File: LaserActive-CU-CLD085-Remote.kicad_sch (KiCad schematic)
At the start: 0 parts

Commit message: Initial start
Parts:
- added C1: 100nF, Capacitor_THT:C_Disc_D4.3mm_W1.9mm_P5.00mm, symbol Device:C_Small
- added C2, C3: 10pF, Capacitor_THT:C_Disc_D3.0mm_W1.6mm_P2.50mm, symbol Device:C_Small
- added C4: 47uF, Capacitor_THT:CP_Radial_D5.0mm_P2.00mm, symbol Device:C_Polarized_Small
- added C5: C_Small, Capacitor_THT:C_Disc_D4.3mm_W1.9mm_P5.00mm, symbol Device:C_Small
- added D1: D_Dual_CommonAnode_AKK, Package_TO_SOT_THT:TO-126-3_Vertical, symbol Device:D_Dual_CommonAnode_AKK
- added D3: IRL81A, LED_THT:LED_SideEmitter_Rectangular_W4.5mm_H1.6mm, symbol LED:IRL81A
- added IC1: D6600CS, Package_DIP:DIP-20_W7.62mm_Socket_LongPads, symbol Pioneer:D6600CS
- added K0, K1, K10, K11, K12, K16, K18, K19, K2, K20, K24, K25, K26, K27, K28, K29, K3, K32, K33, K34, K35, K36, K4, K7: Button, Button_Switch_SMD:SW_SPST_CK_KXT3, symbol Switch:SW_Push
- added Q1: NPN, Package_TO_SOT_THT:TO-220-3_Vertical, symbol Simulation_SPICE:NPN
- added R1: 220, Resistor_THT:R_Axial_DIN0204_L3.6mm_D1.6mm_P5.08mm_Horizontal, symbol Device:R_Small
- added X1: Crystal, Crystal:Crystal_HC18-U_Vertical, symbol Device:Crystal
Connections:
- new net: C3.2, IC1.8 (OSC-IN), X1.1
- new net: C2.2, IC1.7 (OSC-OUT), X1.2
- new net: C1.1, IC1.10 (AC)
- new net: D1.2 (K), IC1.3 (S-IN)
- new net: IC1.5 (REM), Q1.2 (B)
- new net: D3.2 (A), Q1.1 (C)
- new net: D3.1 (K), R1.2
- new net COL_1: IC1.14 (K_I0)
- new net COL_2: IC1.13 (K_I1)
- new net COL_3: IC1.12 (K_I2), K16.1, K18.1, K19.1, K20.1
- new net COL_4: IC1.11 (K_I3)
- new net GND: C1.2, C2.1, C3.1, C4.2, C5.2, IC1.9 (VSS), Q1.3 (E)
- new net ROW_1: IC1.2 (K_IO0)
- new net ROW_2: IC1.1 (K_IO1)
- new net ROW_3: IC1.20 (K_IO2)
- new net ROW_4: IC1.19 (K_IO3), K16.2
- new net ROW_5: IC1.18 (K_IO4)
- new net ROW_6: IC1.17 (K_IO5)
- new net ROW_7: IC1.16 (K_IO6)
- new net ROW_8: IC1.15 (K_IO7)
- new net VCC: C4.1, C5.1, IC1.6 (VDD), R1.1
- no-connect marks 0 -> 1

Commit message: Updates
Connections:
- net COL_1: now also K16.1, K18.1, K19.1, K20.1
- net COL_3: no longer K16.1, K18.1, K19.1, K20.1
- net ROW_1: now also K16.2
- net ROW_2: now also K10.2, K18.2
- net ROW_4: no longer K16.2
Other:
- moved on the sheet: K10, K16, K18, K19, K2, K20
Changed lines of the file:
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@@
 	)
 	(junction
-		(at 154.94 171.45)
+		(at 147.32 114.3)
 		(diameter 0)
 		(color 0 0 0 0)
 	)
 	(junction
-		(at 154.94 149.86)
+		(at 147.32 92.71)
 		(diameter 0)
 		(color 0 0 0 0)
 	)
 	(junction
-		(at 154.94 161.29)
+		(at 147.32 104.14)
 		(diameter 0)
 		(color 0 0 0 0)
@@
 	(wire
 		(pts
-			(xy 154.94 161.29) (xy 154.94 171.45)
+			(xy 147.32 104.14) (xy 147.32 114.3)
 		)
 		(stroke
@@
 	(wire
 		(pts
-			(xy 154.94 171.45) (xy 154.94 181.61)
+			(xy 147.32 114.3) (xy 147.32 124.46)
 		)
 		(stroke
@@
 	(wire
 		(pts
-			(xy 152.4 149.86) (xy 154.94 149.86)
+			(xy 144.78 92.71) (xy 147.32 92.71)
 		)
 		(stroke
@@
 	(wire
 		(pts
-			(xy 154.94 149.86) (xy 154.94 161.29)
+			(xy 147.32 92.71) (xy 147.32 104.14)
 		)
 		(stroke
@@
 		)
 	)
-	(global_label "COL_3"
-		(shape output)
-		(at 152.4 149.86 180)
+	(global_label "COL_1"
+		(shape input)
+		(at 144.78 92.71 180)
 		(fields_autoplaced yes)
 		(effects
@@
 		)
 		(property "Intersheetrefs" "${INTERSHEET_REFS}"
-			(at 143.6091 149.86 0)
+			(at 135.9891 92.71 0)
 			(effects
 				(font
@@
 		)
 	)
+	(global_label "ROW_2"
+		(shape input)
+		(at 186.69 104.14 0)
+		(fields_autoplaced yes)
+		(effects
+			(font
+				(size 1.27 1.27)
+			)
+			(justify left)
+		)
+		(property "Intersheetrefs" "${INTERSHEET_REFS}"
+			(at 195.9042 104.14 0)
+			(effects
+				(font
+					(size 1.27 1.27)
+				)
+				(justify left)
+				(hide yes)
+			)
+		)
+	)
 	(global_label "ROW_7"
 		(shape output)
@@
 		)
 	)
-	(global_label "ROW_4"
+	(global_label "ROW_1"
 		(shape input)
-		(at 165.1 149.86 0)
+		(at 157.48 92.71 0)
 		(fields_autoplaced yes)
 		(effects
@@
 		)
 		(property "Intersheetrefs" "${INTERSHEET_REFS}"
-			(at 174.3142 149.86 0)
+			(at 166.6942 92.71 0)
 			(effects
 				(font
@@
 		)
 	)
+	(global_label "ROW_2"
+		(shape input)
+		(at 157.48 104.14 0)
+		(fields_autoplaced yes)
+		(effects
+			(font
+				(size 1.27 1.27)
+			)
+			(justify left)
+		)
+		(property "Intersheetrefs" "${INTERSHEET_REFS}"
+			(at 166.6942 104.14 0)
+			(effects
+				(font
+					(size 1.27 1.27)
+				)
+				(justify left)
+				(hide yes)
+			)
+		)
+	)
 	(global_label "ROW_1"
 		(shape output)
@@
 	(symbol
 		(lib_id "Switch:SW_Push")
-		(at 160.02 149.86 0)
+		(at 152.4 92.71 0)
 		(unit 1)
 		(exclude_from_sim no)
@@
 		(fields_autoplaced yes)
 		(property "Reference" "K16"
-			(at 160.02 142.24 0)
+			(at 152.4 85.09 0)
 			(effects
 				(font
@@
 		)
 		(property "Value" "Button"
-			(at 160.02 144.78 0)
+			(at 152.4 87.63 0)
 			(effects
 				(font
@@
 		)
 		(property "Footprint" "Button_Switch_SMD:SW_SPST_CK_KXT3"
-			(at 160.02 144.78 0)
+			(at 152.4 87.63 0)
 			(effects
 				(font
@@
 		)
 		(property "Datasheet" "~"
-			(at 160.02 144.78 0)
+			(at 152.4 87.63 0)
 			(effects
 				(font
@@
 		)
 		(property "Description" "Push button switch, generic, two pins"
-			(at 160.02 149.86 0)
+			(at 152.4 92.71 0)
 			(effects
 				(font
@@
 	(symbol
 		(lib_id "Switch:SW_Push")
-		(at 160.02 171.45 0)
+		(at 152.4 114.3 0)
 		(unit 1)
 		(exclude_from_sim no)
@@
 		(fields_autoplaced yes)
 		(property "Reference" "K19"
-			(at 160.02 163.83 0)
+			(at 152.4 106.68 0)
 			(effects
 				(font
@@
 		)
 		(property "Value" "Button"
-			(at 160.02 166.37 0)
+			(at 152.4 109.22 0)
 			(effects
 				(font
@@
 		)
 		(property "Footprint" "Button_Switch_SMD:SW_SPST_CK_KXT3"
-			(at 160.02 166.37 0)
+			(at 152.4 109.22 0)
 			(effects
 				(font
@@
 		)
 		(property "Datasheet" "~"
-			(at 160.02 166.37 0)
+			(at 152.4 109.22 0)
 			(effects
 				(font
@@
 		)
 		(property "Description" "Push button switch, generic, two pins"
-			(at 160.02 171.45 0)
+			(at 152.4 114.3 0)
 			(effects
 				(font
@@
 	(symbol
 		(lib_id "Switch:SW_Push")
-		(at 160.02 181.61 0)
+		(at 152.4 124.46 0)
 		(unit 1)
 		(exclude_from_sim no)
@@
 		(fields_autoplaced yes)
 		(property "Reference" "K20"
-			(at 160.02 173.99 0)
+			(at 152.4 116.84 0)
 			(effects
 				(font
@@
 		)
 		(property "Value" "Button"
-			(at 160.02 176.53 0)
+			(at 152.4 119.38 0)
 			(effects
 				(font
@@
 		)
 		(property "Footprint" "Button_Switch_SMD:SW_SPST_CK_KXT3"
-			(at 160.02 176.53 0)
+			(at 152.4 119.38 0)
 			(effects
 				(font
@@
 		)
 		(property "Datasheet" "~"
-			(at 160.02 176.53 0)
+			(at 152.4 119.38 0)
 			(effects
 				(font
@@
 		)
 		(property "Description" "Push button switch, generic, two pins"
-			(at 160.02 181.61 0)
+			(at 152.4 124.46 0)
 			(effects
 				(font
@@
 	(symbol
 		(lib_id "Switch:SW_Push")
-		(at 72.39 138.43 0)
+		(at 181.61 104.14 0)
 		(unit 1)
 		(exclude_from_sim no)
@@
 		(fields_autoplaced yes)
 		(property "Reference" "K10"
-			(at 72.39 130.81 0)
+			(at 181.61 96.52 0)
 			(effects
 				(font
@@
 		)
 		(property "Value" "Button"
-			(at 72.39 133.35 0)
+			(at 181.61 99.06 0)
 			(effects
 				(font
@@
 		)
 		(property "Footprint" "Button_Switch_SMD:SW_SPST_CK_KXT3"
-			(at 72.39 133.35 0)
+			(at 181.61 99.06 0)
 			(effects
 				(font
@@
 		)
 		(property "Datasheet" "~"
-			(at 72.39 133.35 0)
+			(at 181.61 99.06 0)
 			(effects
 				(font
@@
 		)
 		(property "Description" "Push button switch, generic, two pins"
-			(at 72.39 138.43 0)
+			(at 181.61 104.14 0)
 			(effects
 				(font
@@
 	(symbol
 		(lib_id "Switch:SW_Push")
-		(at 160.02 161.29 0)
+		(at 152.4 104.14 0)
 		(unit 1)
 		(exclude_from_sim no)
@@
 		(fields_autoplaced yes)
 		(property "Reference" "K18"
-			(at 160.02 153.67 0)
+			(at 152.4 96.52 0)
 			(effects
 				(font
@@
 		)
 		(property "Value" "Button"
-			(at 160.02 156.21 0)
+			(at 152.4 99.06 0)
 			(effects
 				(font
@@
 		)
 		(property "Footprint" "Button_Switch_SMD:SW_SPST_CK_KXT3"
-			(at 160.02 156.21 0)
+			(at 152.4 99.06 0)
 			(effects
 				(font
@@
 		)
 		(property "Datasheet" "~"
-			(at 160.02 156.21 0)
+			(at 152.4 99.06 0)
 			(effects
 				(font
@@
 		)
 		(property "Description" "Push button switch, generic, two pins"
-			(at 160.02 161.29 0)
+			(at 152.4 104.14 0)
 			(effects
 				(font
@@
 	(symbol
 		(lib_id "Switch:SW_Push")
-		(at 95.25 138.43 0)
+		(at 208.28 104.14 0)
 		(unit 1)
 		(exclude_from_sim no)
@@
 		(fields_autoplaced yes)
 		(property "Reference" "K2"
-			(at 95.25 130.81 0)
+			(at 208.28 96.52 0)
 			(effects
 				(font
@@
 		)
 		(property "Value" "Button"
-			(at 95.25 133.35 0)
+			(at 208.28 99.06 0)
 			(effects
 				(font
@@
 		)
 		(property "Footprint" "Button_Switch_SMD:SW_SPST_CK_KXT3"
-			(at 95.25 133.35 0)
+			(at 208.28 99.06 0)
 			(effects
 				(font
@@
 		)
 		(property "Datasheet" "~"
-			(at 95.25 133.35 0)
+			(at 208.28 99.06 0)
 			(effects
 				(font
@@
 		)
 		(property "Description" "Push button switch, generic, two pins"
-			(at 95.25 138.43 0)
+			(at 208.28 104.14 0)
 			(effects
 				(font

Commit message: Update LaserActive-CU-CLD085-Remote.kicad_sch
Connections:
- net COL_1: no longer K16.1, K18.1, K19.1, K20.1
- net COL_2: now also K12.2, K20.2, K4.2
- net COL_3: now also K11.1, K19.2, K3.1
- net COL_4: now also K10.2, K18.2, K2.1
- net ROW_1: now also K0.2
- net ROW_2: now also K1.1; no longer K10.2, K18.2
- net ROW_4: now also K16.1, K18.1, K19.1, K20.1
- net ROW_5: now also K10.1, K11.2, K12.1
- net ROW_6: now also K0.1, K1.2, K2.2, K3.2, K4.1
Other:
- moved on the sheet: K0, K1, K10, K11, K12, K16, K18, K19, K2, K20, K3, K4

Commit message: Updates
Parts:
- renumbered C3 to C2, C2 to C3
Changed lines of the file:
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@@
 		(on_board yes)
 		(dnp no)
-		(property "Reference" "C3"
+		(property "Reference" "C2"
 			(at 27.94 76.708 90)
 			(effects
@@
 			(project "LaserActive-CU-CLD085-Remote"
 				(path "/0003d985-390a-41d3-bb3f-5e7567d09c25"
-					(reference "C3")
+					(reference "C2")
 					(unit 1)
 				)
@@
 		(dnp no)
 		(fields_autoplaced yes)
-		(property "Reference" "C2"
+		(property "Reference" "C3"
 			(at 27.9463 58.42 90)
 			(effects
@@
 			(project "LaserActive-CU-CLD085-Remote"
 				(path "/0003d985-390a-41d3-bb3f-5e7567d09c25"
-					(reference "C2")
-					(unit 1)
-				)
+					(reference "C3")
+					(unit 1)
+				)

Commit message: Update Schematics and PCB
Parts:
- added T1, T2: B+, Connector_PinHeader_2.54mm:PinHeader_1x01_P2.54mm_Vertical, symbol Connector_Generic:Conn_01x01
- C4: footprint Capacitor_THT:CP_Radial_D5.0mm_P2.00mm -> Pioneer:Electrolytic_P2.50mm
- IC1: footprint Package_DIP:DIP-20_W7.62mm_Socket_LongPads -> Pioneer:DIP-20_W7.62mm_P1.76mm
- K0, K1, K10, K11, K12, K16, K18, K19, K2, K20, K24, K25, K26, K27, K28, K29, K3, K32, K33, K34, K35, K36, K4, K7: footprint Button_Switch_SMD:SW_SPST_CK_KXT3 -> Pioneer:Button
- Q1: footprint Package_TO_SOT_THT:TO-220-3_Vertical -> Pioneer:TO-220-3
- X1: footprint Crystal:Crystal_HC18-U_Vertical -> Pioneer:Crystal
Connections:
- net ROW_7 is gone; now on net ROW_5: IC1.16 (K_IO6)
- net COL_1: now also IC1.2 (K_IO0), K0.2, K16.2, K24.2, K32.2; no longer IC1.14 (K_I0)
- net COL_2: now also IC1.1 (K_IO1), K1.1, K25.2, K33.1; no longer IC1.13 (K_I1), K12.2, K20.2, K4.2
- net COL_3: now also IC1.11 (K_I3), K10.2, K18.2, K2.1, K26.2, K34.2; no longer IC1.12 (K_I2), K11.1, K19.2, K3.1
- net COL_4: now also IC1.12 (K_I2), K11.1, K19.2, K27.1, K3.1, K35.2; no longer IC1.11 (K_I3), K10.2, K18.2, K2.1
- net GND: now also T2.1 (Pin_1)
- net ROW_1: now also IC1.20 (K_IO2), K24.1, K25.1, K26.1, K27.2, K28.1, K29.2; no longer IC1.2 (K_IO0), K0.2, K16.2
- net ROW_2: now also IC1.19 (K_IO3), K16.1, K18.1, K19.1, K20.1; no longer IC1.1 (K_IO1), K1.1
- net ROW_3: now also IC1.18 (K_IO4), K10.1, K11.2, K12.1; no longer IC1.20 (K_IO2)
- net ROW_4: now also D1.3 (K), IC1.17 (K_IO5), K0.1, K1.2, K2.2, K3.2, K4.1, K7.2; no longer IC1.19 (K_IO3), K16.1, K18.1, K19.1, K20.1
- net ROW_5: now also K7.1; no longer IC1.18 (K_IO4), K10.1, K11.2, K12.1
- net ROW_6: now also D1.2 (K), K32.1, K33.2, K34.1, K35.1, K36.2; no longer IC1.17 (K_IO5), K0.1, K1.2, K2.2, K3.2, K4.1
- net VCC: now also T1.1 (Pin_1)
- net at IC1.3 (S-IN): now also D1.1 (A); no longer D1.2 (K)
- net COL_5: now reaches K28.2
- net COL_5: now also IC1.13 (K_I1), K12.2, K20.2, K36.1, K4.2
- net COL_6: now reaches K29.1
- net COL_6: now also IC1.14 (K_I0)
- net ROW_8: no longer names the net of IC1.15 (K_IO7)
- no-connect marks 1 -> 2
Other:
- moved on the sheet: K0, K1, K10, K11, K12, K16, K18, K19, K2, K20, K24, K25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

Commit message: fix extra b+
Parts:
- T2: value B+ -> B-
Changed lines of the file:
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@@
 			)
 		)
-		(property "Value" "B+"
+		(property "Value" "B-"
 			(at 245.11 80.0099 0)
 			(effects

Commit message: Updates
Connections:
- net at IC1.5 (REM): now also Q1.1 (C); no longer Q1.2 (B)
- net at D3.2 (A): now also Q1.2 (B); no longer Q1.1 (C)
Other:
- moved on the sheet: Q1
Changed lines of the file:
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@@
 	(wire
 		(pts
-			(xy 100.33 67.31) (xy 120.65 67.31)
+			(xy 100.33 67.31) (xy 128.27 67.31)
 		)
 		(stroke
@@
 	(wire
 		(pts
-			(xy 128.27 62.23) (xy 156.21 62.23)
-		)
-		(stroke
-			(width 0)
-			(type default)
-		)
-	)
-	(wire
-		(pts
 			(xy 69.85 57.15) (xy 53.34 57.15)
 		)
@@
 	(wire
 		(pts
+			(xy 135.89 62.23) (xy 156.21 62.23)
+		)
+		(stroke
+			(width 0)
+			(type default)
+		)
+	)
+	(wire
+		(pts
 			(xy 22.86 72.39) (xy 25.4 72.39)
 		)
@@
 		(pts
 			(xy 30.48 64.77) (xy 39.37 64.77)
+		)
+		(stroke
+			(width 0)
+			(type default)
+		)
+	)
+	(wire
+		(pts
+			(xy 135.89 62.23) (xy 135.89 72.39)
 		)
 		(stroke
@@
 	(symbol
 		(lib_id "power:GND")
-		(at 128.27 72.39 0)
+		(at 128.27 77.47 0)
 		(unit 1)
 		(exclude_from_sim no)
@@
 		(fields_autoplaced yes)
 		(property "Reference" "#PWR04"
-			(at 128.27 78.74 0)
+			(at 128.27 83.82 0)
 			(effects
 				(font
@@
 		)
 		(property "Value" "GND"
+			(at 128.27 82.55 0)
+			(effects
+				(font
+					(size 1.27 1.27)
+				)
+			)
+		)
+		(property "Footprint" ""
 			(at 128.27 77.47 0)
 			(effects
@@
 					(size 1.27 1.27)
 				)
-			)
-		)
-		(property "Footprint" ""
-			(at 128.27 72.39 0)
-			(effects
-				(font
-					(size 1.27 1.27)
-				)
 				(hide yes)
 			)
 		)
 		(property "Datasheet" ""
-			(at 128.27 72.39 0)
+			(at 128.27 77.47 0)
 			(effects
 				(font
@@
 		)
 		(property "Description" "Power symbol creates a global label with name \"GND\" , ground"
-			(at 128.27 72.39 0)
+			(at 128.27 77.47 0)
 			(effects
 				(font
@@
 	(symbol
 		(lib_id "Simulation_SPICE:NPN")
-		(at 125.73 67.31 0)
+		(at 130.81 72.39 0)
+		(mirror y)
 		(unit 1)
 		(exclude_from_sim no)
@@
 		(on_board yes)
 		(dnp no)
-		(fields_autoplaced yes)
 		(property "Reference" "Q1"
-			(at 130.81 66.0399 0)
+			(at 125.73 71.1199 0)
 			(effects
 				(font
@@
 		)
 		(property "Value" "NPN"
-			(at 130.81 68.5799 0)
+			(at 125.73 73.6599 0)
 			(effects
 				(font
@@
 		)
 		(property "Footprint" "Pioneer:TO-220-3"
-			(at 189.23 67.31 0)
+			(at 67.31 72.39 0)
 			(effects
 				(font
@@
 		)
 		(property "Datasheet" ""
-			(at 189.23 67.31 0)
+			(at 67.31 72.39 0)
 			(effects
 				(font
@@
 		)
 		(property "Description" ""
-			(at 125.73 67.31 0)
+			(at 130.81 72.39 0)
 			(effects
 				(font
@@
 		)
 		(property "Sim.Device" "NPN"
-			(at 125.73 67.31 0)
+			(at 130.81 72.39 0)
 			(effects
 				(font
@@
 		)
 		(property "Sim.Type" "GUMMELPOON"
-			(at 125.73 67.31 0)
+			(at 130.81 72.39 0)
 			(effects
 				(font
@@
 		)
 		(property "Sim.Pins" "1=C 2=B 3=E"
-			(at 125.73 67.31 0)
-			(effects
-				(font
+			(at 130.81 72.39 0)
+			(effects
+				(font

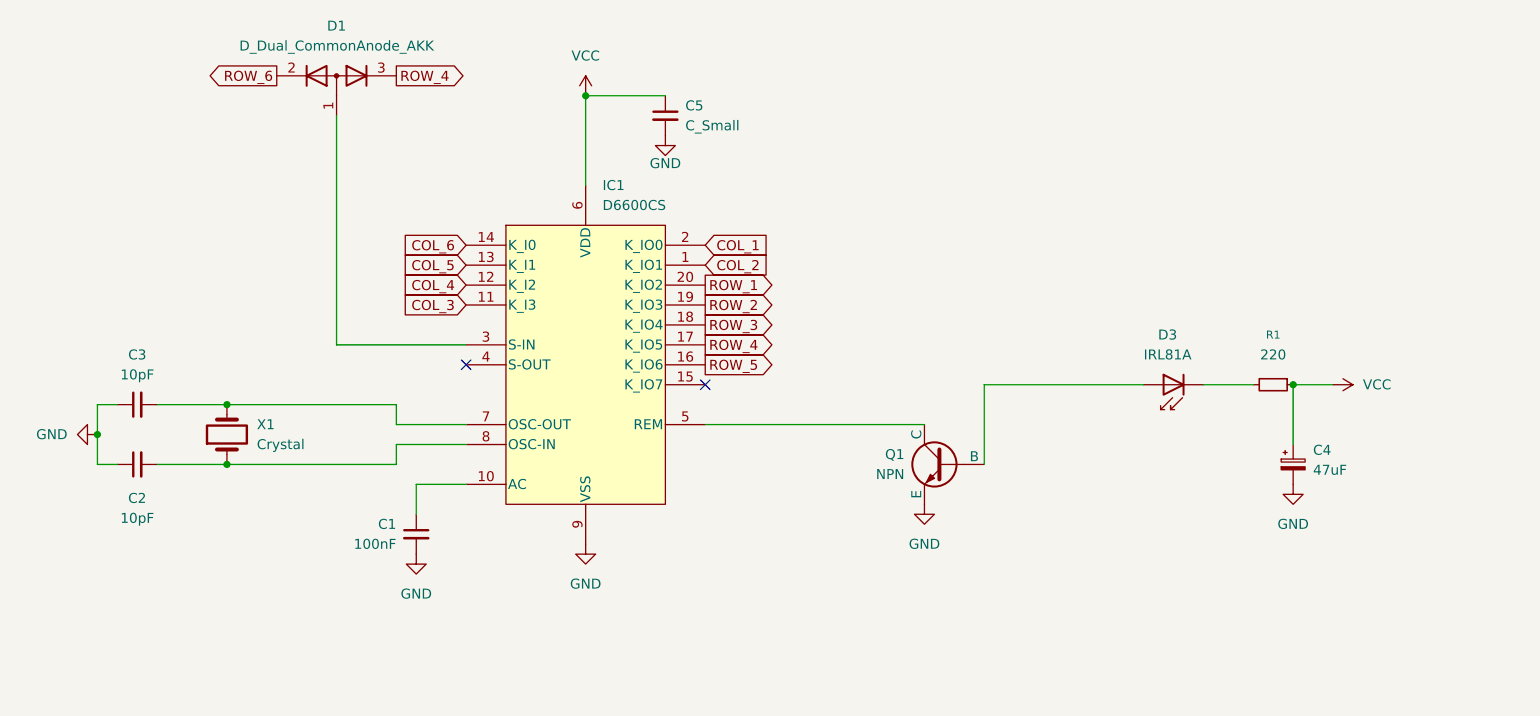
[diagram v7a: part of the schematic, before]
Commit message: Fix Schematic Values and symbols
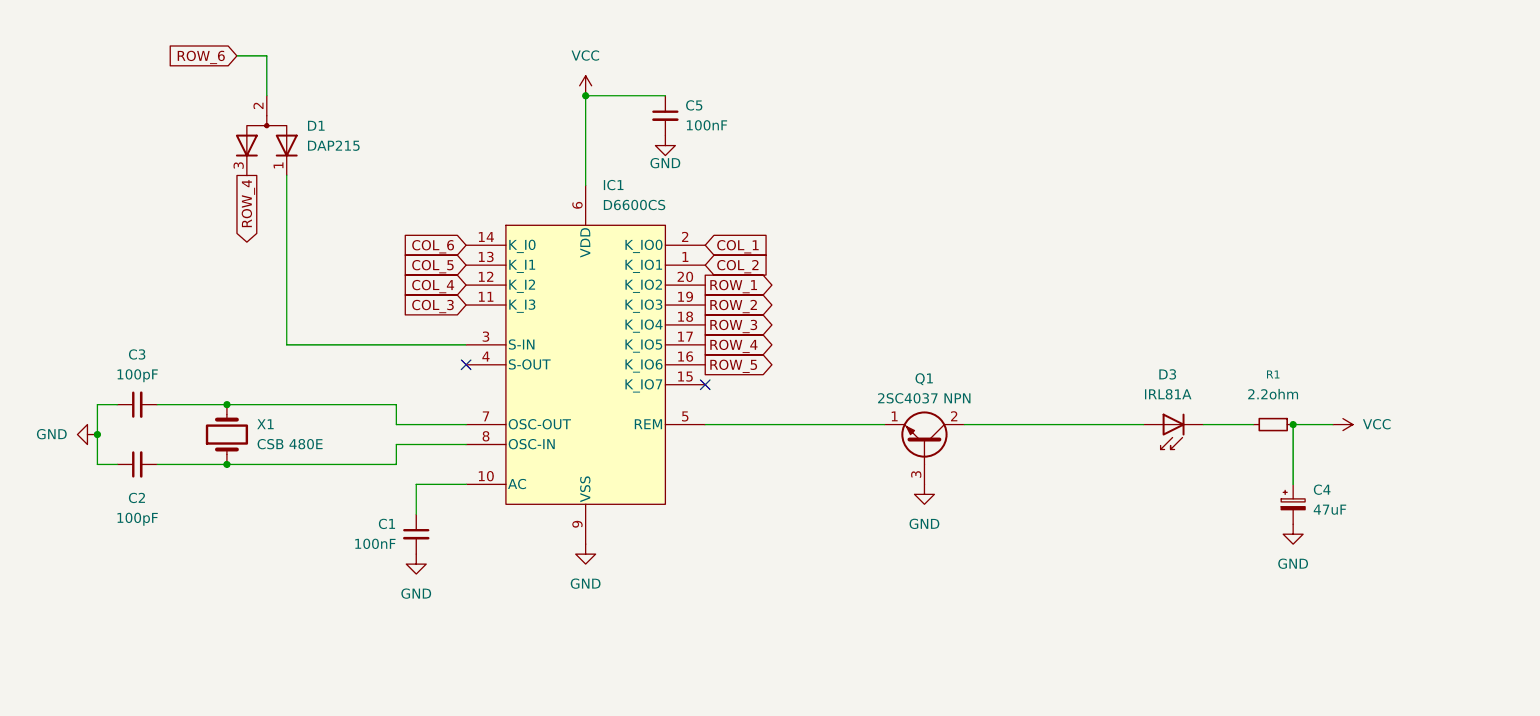
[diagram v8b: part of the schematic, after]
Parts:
- C2, C3: value 10pF -> 100pF
- C5: value C_Small -> 100nF
- D1: value D_Dual_CommonAnode_AKK -> DAP215; symbol Device:D_Dual_CommonAnode_AKK -> Device:D_Dual_CommonAnode_KAK_Parallel
- Q1: value NPN -> 2SC4037 NPN; symbol Simulation_SPICE:NPN -> Transistor_BJT:BF457
- R1: value 220 -> 2.2ohm
- X1: value Crystal -> CSB 480E
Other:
- moved on the sheet: C4, D1, D3, R1
